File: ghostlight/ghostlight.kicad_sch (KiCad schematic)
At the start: 0 parts

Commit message: added first scheme for the board
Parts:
- added BT1: 3000, 3000, symbol SamacSys_Parts:3000
- added C1, C2: MBASG168AB7105KTNA01, MBASx168, symbol SamacSys_Parts:MBASG168AB7105KTNA01
- added IC2: MCP1700T-3302E_TT, SOT95P237X112-3N, symbol SamacSys_Parts:MCP1700T-3302E_TT
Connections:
- new net 3.3V: C2.2, IC2.2 (VOUT)
- new net GND: BT1.3 (-), C1.1, C2.1, IC2.1 (GND)
- new net V_BAT: BT1.1 (+_1), BT1.2 (+_2), C1.2, IC2.3 (VIN)

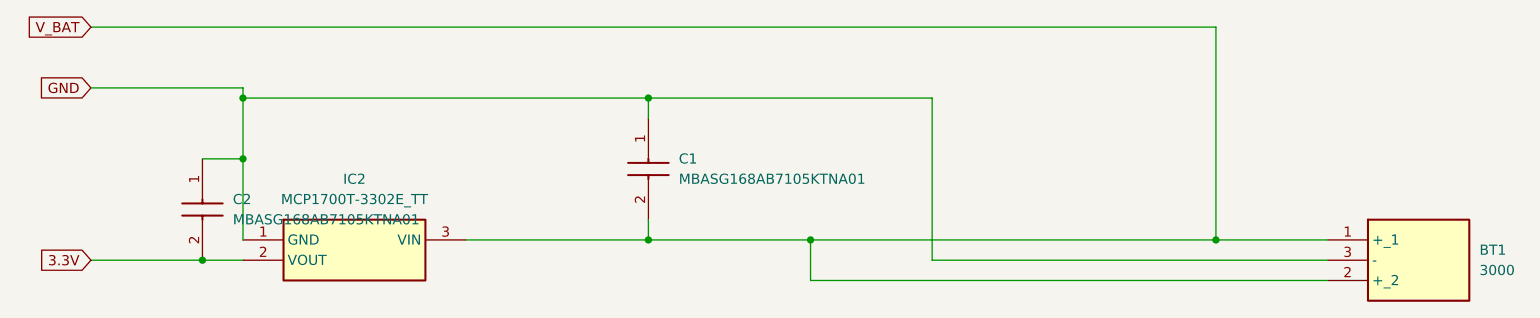
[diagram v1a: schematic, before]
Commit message: Add new battery holder
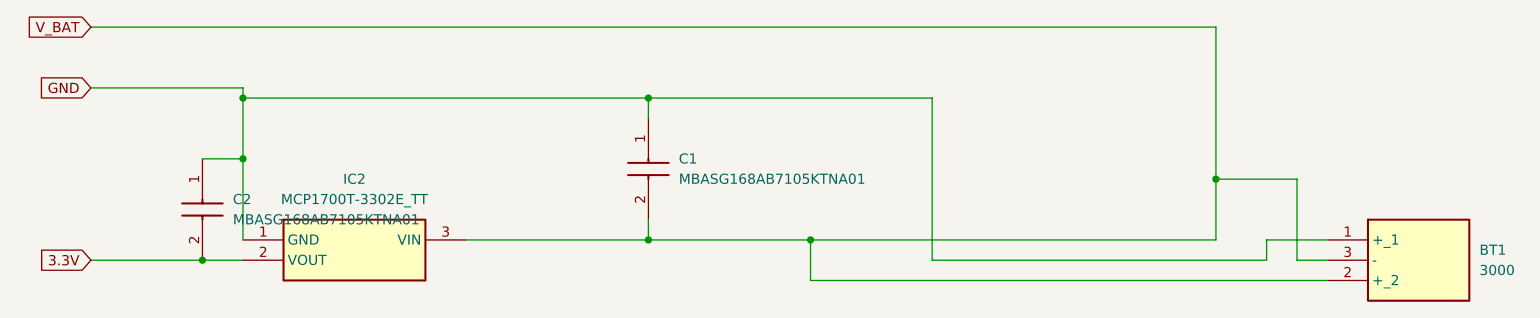
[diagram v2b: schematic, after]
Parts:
- BT1: footprint 3000 -> custom_ring:Battery_Holder_Lynx_CR2032
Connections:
- net GND: now also BT1.1 (+_1); no longer BT1.3 (-)
- net V_BAT: now also BT1.3 (-); no longer BT1.1 (+_1)
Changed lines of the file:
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@@
 	(paper "A4")
+	(junction
+		(at 208.28 111.76)
+		(diameter 0)
+		(color 0 0 0 0)
+	)
 	(junction
 		(at 157.48 119.38)
@@
 	)
 	(junction
-		(at 208.28 119.38)
-		(diameter 0)
-		(color 0 0 0 0)
-	)
-	(junction
 		(at 86.36 101.6)
 		(diameter 0)
@@
 	(wire
 		(pts
-			(xy 208.28 119.38) (xy 222.25 119.38)
-		)
-		(stroke
-			(width 0)
-			(type default)
-		)
-	)
-	(wire
-		(pts
 			(xy 222.25 124.46) (xy 157.48 124.46)
 		)
@@
 	(wire
 		(pts
+			(xy 208.28 111.76) (xy 208.28 119.38)
+		)
+		(stroke
+			(width 0)
+			(type default)
+		)
+	)
+	(wire
+		(pts
+			(xy 214.63 121.92) (xy 214.63 119.38)
+		)
+		(stroke
+			(width 0)
+			(type default)
+		)
+	)
+	(wire
+		(pts
+			(xy 222.25 121.92) (xy 218.44 121.92)
+		)
+		(stroke
+			(width 0)
+			(type default)
+		)
+	)
+	(wire
+		(pts
 			(xy 86.36 100.33) (xy 86.36 101.6)
 		)
@@
 	(wire
 		(pts
-			(xy 172.72 121.92) (xy 222.25 121.92)
-		)
-		(stroke
-			(width 0)
-			(type default)
-		)
-	)
-	(wire
-		(pts
 			(xy 86.36 101.6) (xy 137.16 101.6)
 		)
@@
 	(wire
 		(pts
+			(xy 218.44 111.76) (xy 208.28 111.76)
+		)
+		(stroke
+			(width 0)
+			(type default)
+		)
+	)
+	(wire
+		(pts
 			(xy 137.16 101.6) (xy 172.72 101.6)
 		)
@@
 	(wire
 		(pts
+			(xy 214.63 119.38) (xy 222.25 119.38)
+		)
+		(stroke
+			(width 0)
+			(type default)
+		)
+	)
+	(wire
+		(pts
+			(xy 172.72 121.92) (xy 214.63 121.92)
+		)
+		(stroke
+			(width 0)
+			(type default)
+		)
+	)
+	(wire
+		(pts
+			(xy 218.44 121.92) (xy 218.44 111.76)
+		)
+		(stroke
+			(width 0)
+			(type default)
+		)
+	)
+	(wire
+		(pts
 			(xy 137.16 116.84) (xy 137.16 119.38)
 		)
@@
 	(wire
 		(pts
-			(xy 208.28 92.71) (xy 208.28 119.38)
+			(xy 208.28 92.71) (xy 208.28 111.76)
 		)
 		(stroke
@@
 			)
 		)
-		(property "Footprint" "3000"
+		(property "Footprint" "custom_ring:Battery_Holder_Lynx_CR2032"
 			(at 241.3 214.3 0)
 			(hide yes)
